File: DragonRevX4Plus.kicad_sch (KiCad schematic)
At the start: 5 parts, among them J3 Board Interconnect Female, J4 Conn_02x08_Odd_Even, J5 Video Output Female

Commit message: Progress routing
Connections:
- net DC0 renamed D0
- net DC1 renamed D1
- net DC2 renamed D2
- net DC3 renamed D3
- net DC4 renamed D4
- net DC5 renamed D5
- net DC6 renamed D6
- net DC7 renamed D7
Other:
- sheet SAM ports: added DO[0..7]; removed none
- moved on the sheet: J3, J4

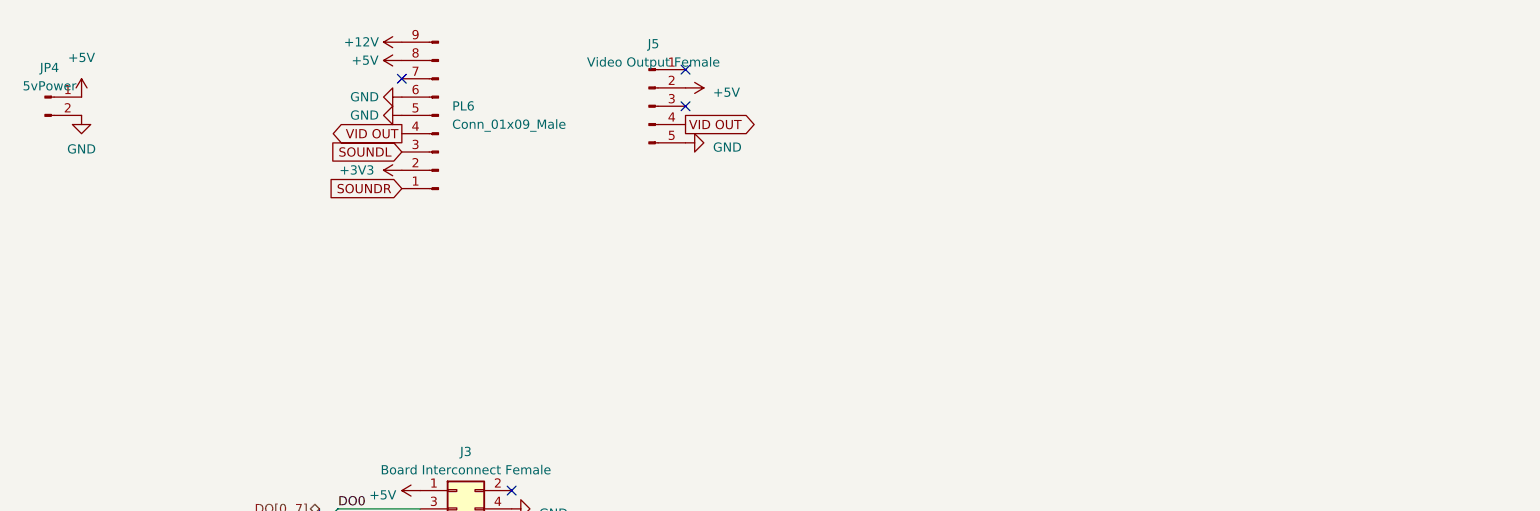
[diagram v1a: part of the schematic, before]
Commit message: rework to flex atx size
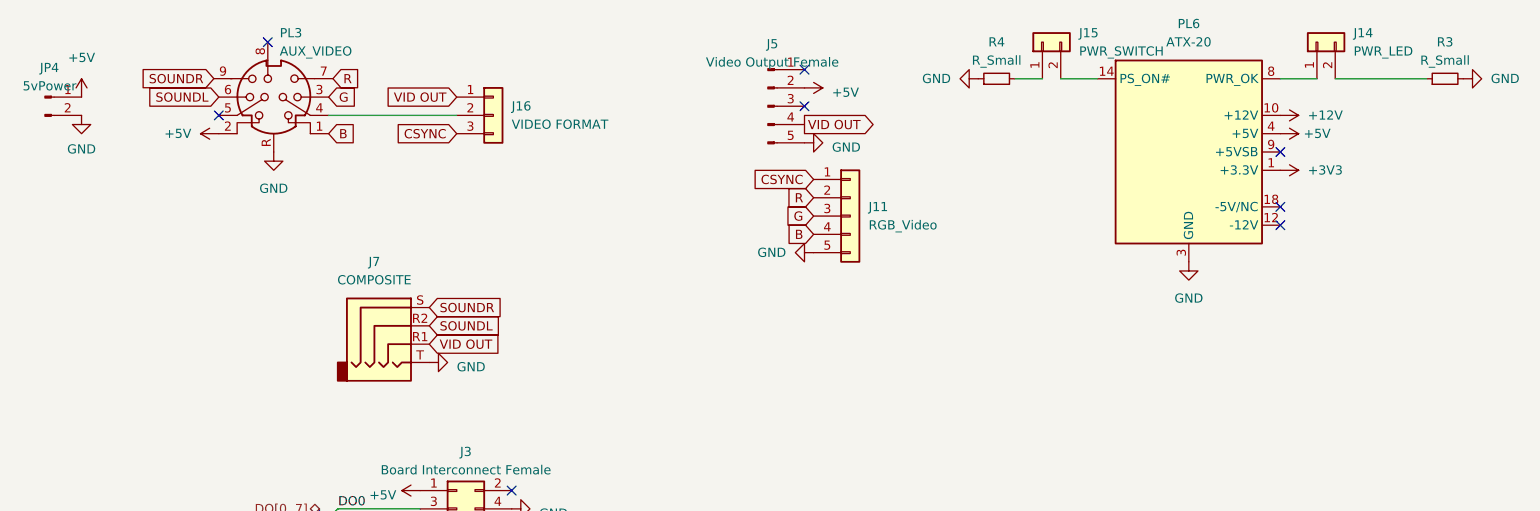
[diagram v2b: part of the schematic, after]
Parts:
- removed PL6: Conn_01x09_Male, Connector_Molex:Molex_KK-396_A-41791-0009_1x09_P3.96mm_Vertical, symbol Connector:Conn_01x09_Male
- added J11: RGB_Video, Connector_PinHeader_2.54mm:PinHeader_1x05_P2.54mm_Vertical, symbol Connector_Generic:Conn_01x05
- added J14: PWR_LED, Connector_PinHeader_2.54mm:PinHeader_1x02_P2.54mm_Vertical, symbol Connector_Generic:Conn_01x02
- added J15: PWR_SWITCH, Connector_PinHeader_2.54mm:PinHeader_1x02_P2.54mm_Vertical, symbol Connector_Generic:Conn_01x02
- added J16: VIDEO FORMAT, Connector_PinHeader_2.54mm:PinHeader_1x03_P2.54mm_Vertical, symbol Connector_Generic:Conn_01x03
- added J7: COMPOSITE, Connector_Audio:Jack_3.5mm_PJ320E_Horizontal, symbol Connector_Audio:AudioJack4
- added PL3: AUX_VIDEO, CoCoDragonMultiPak:KMDGX-9S-N, symbol vdg:Mini-DIN-9R
- added PL6: ATX-20, Connector_Molex:Molex_Mini-Fit_Jr_5566-20A_2x10_P4.20mm_Vertical, symbol Connector:ATX-20
- added R3, R4: R_Small, Resistor_SMD:R_0805_2012Metric_Pad1.20x1.40mm_HandSolder, symbol Device:R_Small
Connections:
- net +12V: now also PL6.10 (+12V)
- net +3V3: now also PL6.1 (+3.3V), PL6.11 (+3.3V), PL6.2 (+3.3V)
- net +5V: now also PL3.2, PL6.19 (+5V), PL6.20 (+5V), PL6.4 (+5V), PL6.6 (+5V)
- net GND: now also J11.5 (Pin_5), J7.T, PL3.R, PL6.13 (GND), PL6.15 (GND), PL6.16 (GND), PL6.17 (GND), PL6.3 (GND), PL6.5 (GND), PL6.7 (GND), R3.2, R4.1
- net SOUNDL: now also J7.R2, PL3.6
- net SOUNDR: now also J7.S, PL3.9
- net VID OUT: now also J16.1 (Pin_1), J7.R1
- new net: J15.2 (Pin_2), PL6.14 (PS_ON#)
- new net: J14.1 (Pin_1), PL6.8 (PWR_OK)
- new net: J16.2 (Pin_2), PL3.4
- new net: J14.2 (Pin_2), R3.1
- new net: J15.1 (Pin_1), R4.2
- new net B: J11.4 (Pin_4), PL3.1
- new net CSYNC: J11.1 (Pin_1), J16.3 (Pin_3)
- new net G: J11.3 (Pin_3), PL3.3
- new net R: J11.2 (Pin_2), PL3.7
- no-connect marks 5 -> 9
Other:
- moved on the sheet: J5

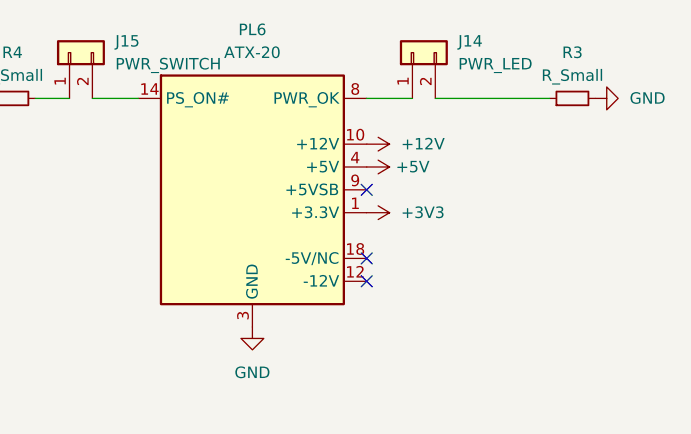
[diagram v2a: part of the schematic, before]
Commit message: complete routing
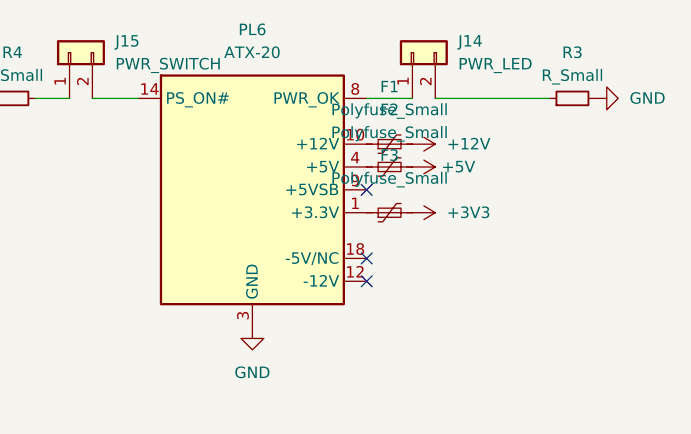
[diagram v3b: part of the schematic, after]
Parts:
- added F1, F2, F3: Polyfuse_Small, Fuse:Fuse_Bourns_MF-RHT400, symbol Device:Polyfuse_Small
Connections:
- net +12V: now also F1.2; no longer PL6.10 (+12V)
- net +3V3: now also F3.2; no longer PL6.1 (+3.3V), PL6.11 (+3.3V), PL6.2 (+3.3V)
- net +5V: now also F2.2; no longer PL6.19 (+5V), PL6.20 (+5V), PL6.4 (+5V), PL6.6 (+5V)
- new net: F3.1, PL6.1 (+3.3V), PL6.11 (+3.3V), PL6.2 (+3.3V)
- new net: F2.1, PL6.19 (+5V), PL6.20 (+5V), PL6.4 (+5V), PL6.6 (+5V)
- new net: F1.1, PL6.10 (+12V)

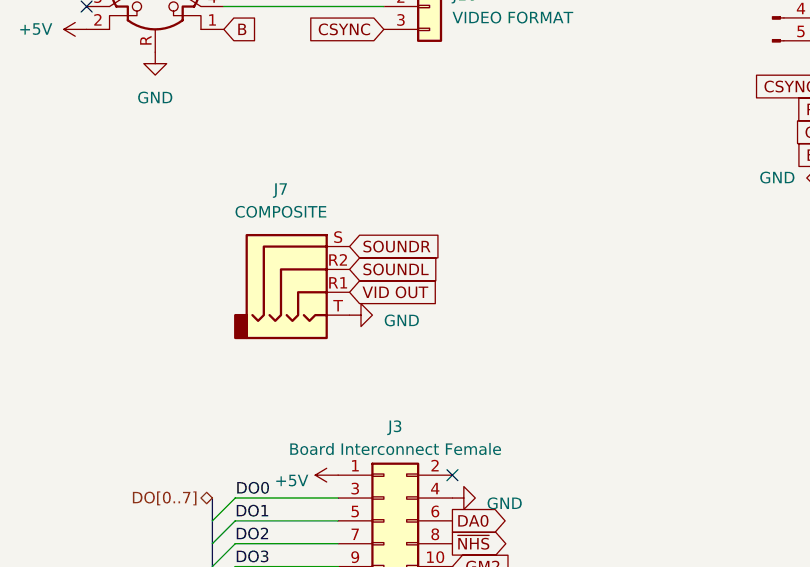
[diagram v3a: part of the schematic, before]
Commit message: fix 3.5mm video wiring
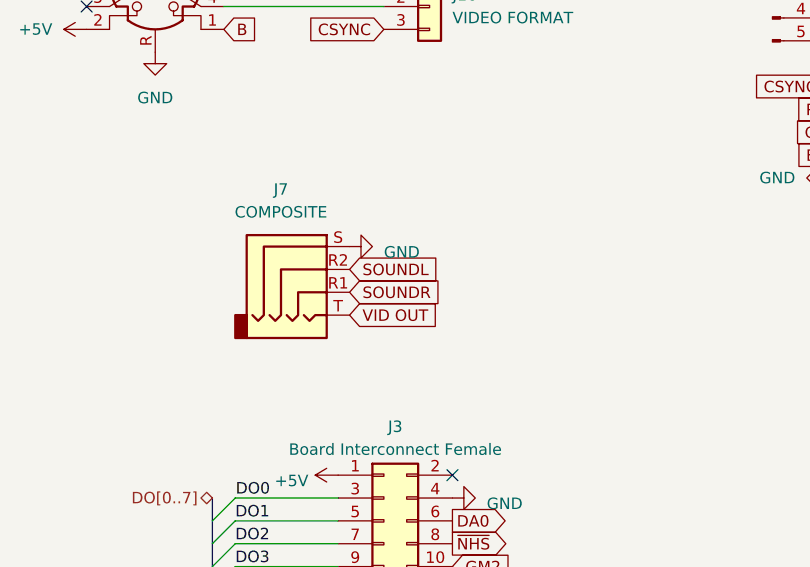
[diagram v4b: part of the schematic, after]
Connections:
- net GND: now also J7.S; no longer J7.T
- net SOUNDR: now also J7.R1; no longer J7.S
- net VID OUT: now also J7.T; no longer J7.R1

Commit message: add isa style slots
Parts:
- removed J11: RGB_Video, Connector_PinHeader_2.54mm:PinHeader_1x05_P2.54mm_Vertical, symbol Connector_Generic:Conn_01x05
- removed J16: VIDEO FORMAT, Connector_PinHeader_2.54mm:PinHeader_1x03_P2.54mm_Vertical, symbol Connector_Generic:Conn_01x03
- removed J3: Board Interconnect Female, Connector_PinSocket_2.54mm:PinSocket_2x11_P2.54mm_Vertical, symbol Connector_Generic:Conn_02x11_Odd_Even
- removed J4: Conn_02x08_Odd_Even, Connector_PinSocket_2.54mm:PinSocket_2x08_P2.54mm_Vertical, symbol Connector_Generic:Conn_02x08_Odd_Even
- removed J5: Video Output Female, Connector_PinSocket_2.54mm:PinSocket_1x05_P2.54mm_Vertical, symbol Connector:Conn_01x05_Pin
- removed PL3: AUX_VIDEO, CoCoDragonMultiPak:KMDGX-9S-N, symbol vdg:Mini-DIN-9R
- added PL1, PL10, PL4, PL9: ~, Dragon:ISA_2x31, symbol vdg:XT8
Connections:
- net +12V: now also PL1.b9 (+12V), PL10.b9 (+12V), PL4.b9 (+12V), PL9.b9 (+12V)
- net +3V3: now also PL1.b7 (-12V), PL10.b7 (-12V), PL4.b7 (-12V), PL9.b7 (-12V)
- net +5V: now also PL1.b29 (+5V), PL1.b3 (+5V), PL10.b29 (+5V), PL10.b3 (+5V), PL4.b29 (+5V), PL4.b3 (+5V), PL9.b29 (+5V), PL9.b3 (+5V)
- net CSS: now also PL1.a12 (A19)
- net D0: now also PL1.a9 (D0), PL10.a9 (D0), PL4.a9 (D0), PL9.a9 (D0)
- net D1: now also PL1.a8 (D1), PL10.a8 (D1), PL4.a8 (D1), PL9.a8 (D1)
- net D2: now also PL1.a7 (D2), PL10.a7 (D2), PL4.a7 (D2), PL9.a7 (D2)
- net D3: now also PL1.a6 (D3), PL10.a6 (D3), PL4.a6 (D3), PL9.a6 (D3)
- net D4: now also PL1.a5 (D4), PL10.a5 (D4), PL4.a5 (D4), PL9.a5 (D4)
- net D5: now also PL1.a4 (D5), PL10.a4 (D5), PL4.a4 (D5), PL9.a4 (D5)
- net D6: now also PL1.a3 (D6), PL10.a3 (D6), PL4.a3 (D6), PL9.a3 (D6)
- net D7: now also PL1.a2 (D7), PL10.a2 (D7), PL4.a2 (D7), PL9.a2 (D7)
- net DA0: now also PL1.a15 (A16)
- net DO0: now also PL1.b19 (~{REFRESH}), PL10.b19 (~{REFRESH}), PL4.b19 (~{REFRESH}), PL9.b19 (~{REFRESH})
- net DO1: now also PL1.b18 (DRQ1), PL10.b18 (DRQ1), PL4.b18 (DRQ1), PL9.b18 (DRQ1)
- net DO2: now also PL1.b17 (~{DACK1}), PL10.b17 (~{DACK1}), PL4.b17 (~{DACK1}), PL9.b17 (~{DACK1})
- net DO3: now also PL1.b16 (DRQ3), PL10.b16 (DRQ3), PL4.b16 (DRQ3), PL9.b16 (DRQ3)
- net DO4: now also PL1.b15 (~{DACK3}), PL10.b15 (~{DACK3}), PL4.b15 (~{DACK3}), PL9.b15 (~{DACK3})
- net DO5: now also PL1.b14 (~{IOR}), PL10.b14 (~{IOR}), PL4.b14 (~{IOR}), PL9.b14 (~{IOR})
- net DO6: now also PL1.b13 (~{IOW}), PL10.b13 (~{IOW}), PL4.b13 (~{IOW}), PL9.b13 (~{IOW})
- net DO7: now also PL1.b12 (~{SMEMR}), PL10.b12 (~{SMEMR}), PL4.b12 (~{SMEMR}), PL9.b12 (~{SMEMR})
- net E: now also PL1.b20 (CLK), PL10.b20 (CLK), PL4.b20 (CLK), PL9.b20 (CLK)
- net GM0: now also PL1.b28 (ALE)
- net GM1: now also PL1.b27 (T/C)
- net GM2: now also PL1.b26 (~{DACK2})
- net GND: now also PL1.b1 (GND), PL1.b10 (GND), PL1.b31 (GND), PL10.b1 (GND), PL10.b10 (GND), PL10.b31 (GND), PL4.b1 (GND), PL4.b10 (GND), PL4.b31 (GND), PL9.b1 (GND), PL9.b10 (GND), PL9.b31 (GND)
- net P1b: now also PL1.b22 (IRQ6)
- net R/~{W}: now also PL1.b11 (~{SMEMW}), PL10.b11 (~{SMEMW}), PL4.b11 (~{SMEMW}), PL9.b11 (~{SMEMW})
- net VCLK: now also PL1.b30 (OSC), PL10.b30 (OSC), PL4.b30 (OSC), PL9.b30 (OSC)
- net VID OUT: now also PL1.a11 (AEN)
- net ~{A}/G: now also PL1.a13 (A18)
- net ~{FS}: now also PL1.b8 (~{NOWS})
- net ~{NHS}: now also PL1.b6 (DRQ2)
- net ~{RAS0}: now also PL1.a14 (A17), PL10.a14 (A17), PL4.a14 (A17), PL9.a14 (A17)
- new net A0: PL1.a31 (A0), PL10.a31 (A0), PL4.a31 (A0), PL9.a31 (A0)
- new net A1: PL1.a30 (A1), PL10.a30 (A1), PL4.a30 (A1), PL9.a30 (A1)
- new net A10: PL1.a21 (A10), PL10.a21 (A10), PL4.a21 (A10), PL9.a21 (A10)
- new net A11: PL1.a20 (A11), PL10.a20 (A11), PL4.a20 (A11), PL9.a20 (A11)
- new net A12: PL1.a19 (A12), PL10.a19 (A12), PL4.a19 (A12), PL9.a19 (A12)
- new net A13: PL1.a18 (A13), PL10.a18 (A13), PL4.a18 (A13), PL9.a18 (A13)
- new net A14: PL1.a17 (A14), PL10.a17 (A14), PL4.a17 (A14), PL9.a17 (A14)
- new net A15: PL1.a16 (A15), PL10.a16 (A15), PL4.a16 (A15), PL9.a16 (A15)
- new net A2: PL1.a29 (A2), PL10.a29 (A2), PL4.a29 (A2), PL9.a29 (A2)
- new net A3: PL1.a28 (A3), PL10.a28 (A3), PL4.a28 (A3), PL9.a28 (A3)
- new net A4: PL1.a27 (A4), PL10.a27 (A4), PL4.a27 (A4), PL9.a27 (A4)
- new net A5: PL1.a26 (A5), PL10.a26 (A5), PL4.a26 (A5), PL9.a26 (A5)
- new net A6: PL1.a25 (A6), PL10.a25 (A6), PL4.a25 (A6), PL9.a25 (A6)
- new net A7: PL1.a24 (A7), PL10.a24 (A7), PL4.a24 (A7), PL9.a24 (A7)
- new net A8: PL1.a23 (A8), PL10.a23 (A8), PL4.a23 (A8), PL9.a23 (A8)
- new net A9: PL1.a22 (A9), PL10.a22 (A9), PL4.a22 (A9), PL9.a22 (A9)
- new net OUT_A: PL4.b26 (~{DACK2})
- new net OUT_B: PL4.b27 (T/C)
- new net OUT_C: PL4.b28 (ALE)
- new net OUT_D: PL4.a11 (AEN)
- new net OUT_E: PL4.a12 (A19)
- new net OUT_F: PL4.a13 (A18)
- new net P1a: PL1.b21 (IRQ7)
- new net P1c: PL4.b21 (IRQ7)
- new net P1d: PL4.b22 (IRQ6)
- new net P1e: PL9.b21 (IRQ7)
- new net P1f: PL9.b22 (IRQ6)
- new net P1g: PL10.b21 (IRQ7)
- new net P1h: PL10.b22 (IRQ6)
- new net ~{FIRQ}: PL1.b23 (IRQ5), PL10.b23 (IRQ5), PL4.b23 (IRQ5), PL9.b23 (IRQ5)
- new net ~{HALT}: PL1.b4 (IRQ2), PL10.b4 (IRQ2), PL4.b4 (IRQ2), PL9.b4 (IRQ2)
- new net ~{IRQ}: PL1.b24 (IRQ4), PL10.b24 (IRQ4), PL4.b24 (IRQ4), PL9.b24 (IRQ4)
- new net ~{NMI}: PL1.b25 (IRQ3), PL10.b25 (IRQ3), PL4.b25 (IRQ3), PL9.b25 (IRQ3)
- new net ~{RES}: PL1.b2 (RESET), PL10.b2 (RESET), PL4.b2 (RESET), PL9.b2 (RESET)
- no-connect marks 9 -> 32
